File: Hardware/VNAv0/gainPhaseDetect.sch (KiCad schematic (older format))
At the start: 34 parts, among them U14 F2923, U15 AD8302

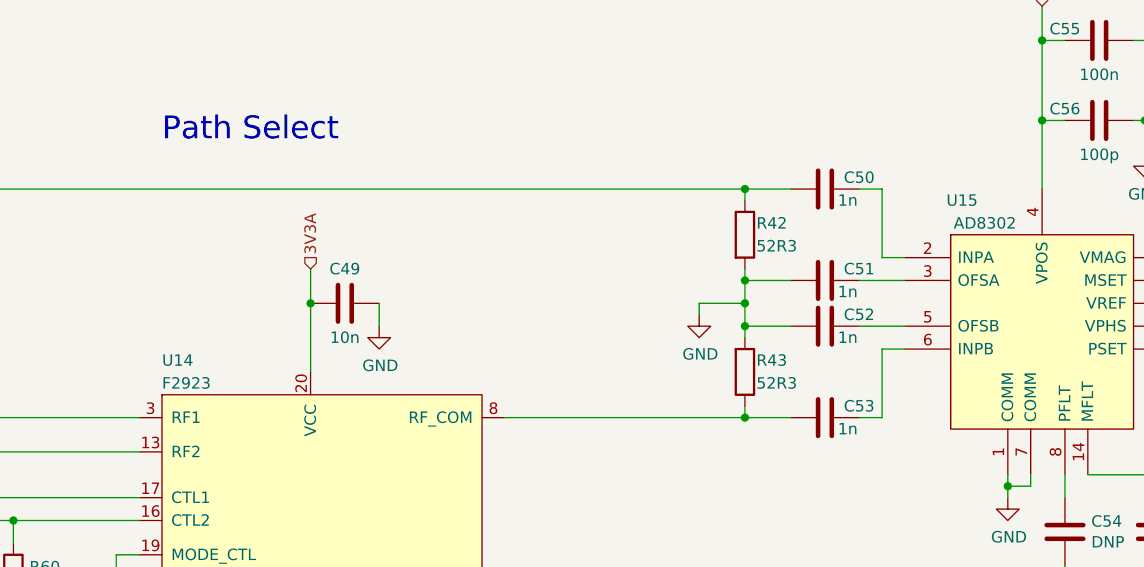
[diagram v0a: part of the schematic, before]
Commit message: tx chain now works, however output power too low
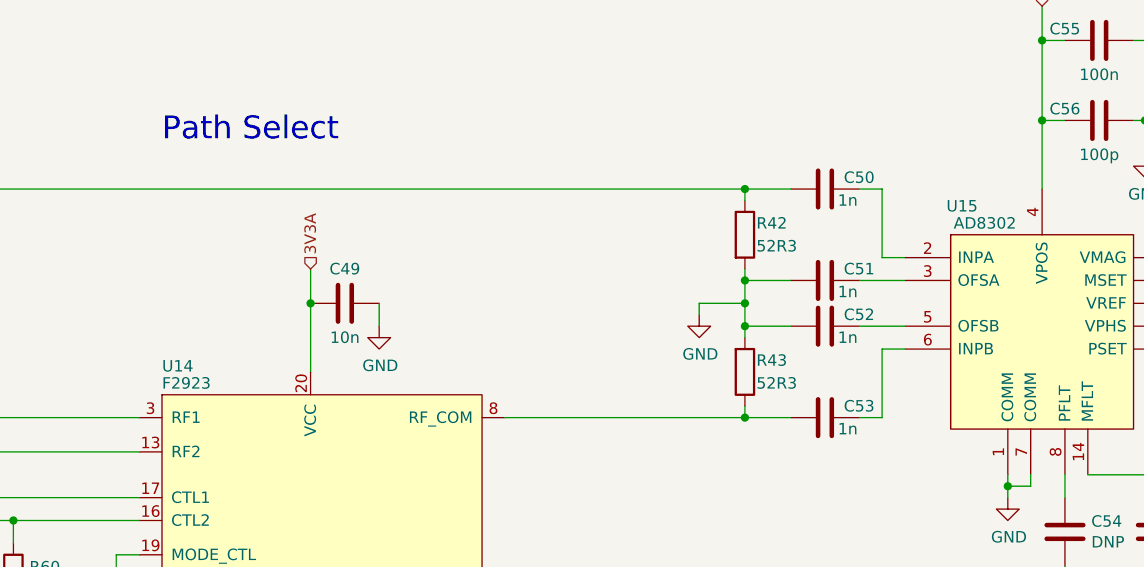
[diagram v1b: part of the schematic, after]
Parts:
- U14: footprint VNA_Footprints:QFN-20-1EP_4x4mm_P0.5mm_EP2x2mm_ThermalVias -> (none)
- U15: footprint Package_SO:TSSOP-14_4.4x5mm_P0.65mm -> (none)
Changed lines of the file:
@@
-$EndComp
-$Comp
-L VNA_Symbols:AD8302 U15
-U 1 1 5CDA92FC
-P 7500 3300
-F 0 "U15" H 7750 3550 50  0000 C CNN
-F 1 "AD8302" H 7850 3450 50  0000 C CNN
-F 2 "Package_SO:TSSOP-14_4.4x5mm_P0.65mm" H 8550 3400 50  0001 L CNN
-F 3 "" H 8550 3300 50  0001 L CNN
-	1    7500 3300
-	1    0    0    -1
 $EndComp
 $Comp
@@
 Wire Wire Line
 	9700 3600 9800 3600
-$Comp
-L VNA_Symbols:F2923 U14
-U 1 1 5CC05CAB
-P 4900 4350
-F 0 "U14" H 4250 4950 50  0000 L CNN
-F 1 "F2923" H 4250 4850 50  0000 L CNN
-F 2 "VNA_Footprints:QFN-20-1EP_4x4mm_P0.5mm_EP2x2mm_ThermalVias" H 4900 4850 50  0001 C CNN
-F 3 "" H 4900 4850 50  0001 C CNN
-	1    4900 4350
-	1    0    0    -1
-$EndComp
 Wire Wire Line
 	2700 4150 2700 5000
@@
 	2700 5000 2300 5000
 Connection ~ 2300 5000
+$Comp
+L VNA_Symbols:AD8302 U15
+U 1 1 5D17A3F6
+P 7500 3300
+F 0 "U15" H 7750 3525 50  0000 C CNN
+F 1 "AD8302" H 7850 3450 50  0000 C CNN
+F 2 "" H 8550 3400 50  0001 L CNN
+F 3 "" H 8550 3300 50  0001 L CNN
+	1    7500 3300
+	1    0    0    -1
+$EndComp
+$Comp
+L VNA_Symbols:F2923 U14
+U 1 1 5D17C1EF
+P 4900 4350
+F 0 "U14" H 4250 4925 50  0000 L CNN
+F 1 "F2923" H 4250 4850 50  0000 L CNN
+F 2 "" H 4900 4850 50  0001 C CNN
+F 3 "" H 4900 4850 50  0001 C CNN
+	1    4900 4350
+	1    0    0    -1
+$EndComp
 $EndSCHEMATC
